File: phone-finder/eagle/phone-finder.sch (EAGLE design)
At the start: 52 parts, among them J1 MICRO USB, J2 SWD HEADER, K1 35701331, Q1 12Mhz, Q2 2N2222, Q3 2N2222, T1 DTA114EET1G (2x10K), U1 AP2114H-3.3TRG1, U2 NUF2042XV6T1G, U3 LPC11U35FHI33/501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

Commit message: Work in progress
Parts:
- Q2: device transistor-npn:BC818-16SMD -> transistor-npn:BC847ALT1SMD
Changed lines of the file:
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@@
 <part name="R12" library="wifi-orb" deviceset="R-US_" device="R0402" value="100"/>
 <part name="R9" library="wifi-orb" deviceset="R-US_" device="R0402" value="100"/>
-<part name="Q2" library="transistor-npn" deviceset="BC818*" device="SMD" technology="-16" value="2N2222"/>
 <part name="+5V4" library="wifi-orb" deviceset="+5V" device=""/>
 <part name="C15" library="wifi-orb" deviceset="CAPACITOR" device="C0603K" value="0.1uF"/>
@@
 <part name="R8" library="wifi-orb" deviceset="R-US_" device="R0402" value="3K"/>
 <part name="C16" library="wifi-orb" deviceset="CAPACITOR" device="C0603K" value="0.1uF"/>
+<part name="Q2" library="transistor-npn" deviceset="BC847*" device="SMD" technology="ALT1" value="2N2222"/>
 </parts>
 <sheets>
@@
 <attribute name="VALUE" x="293.37" y="124.206" size="1.778" layer="96"/>
 </instance>
-<instance part="Q2" gate="G$1" x="297.18" y="132.08" smashed="yes">
-<attribute name="NAME" x="301.752" y="134.112" size="1.778" layer="95"/>
-<attribute name="VALUE" x="301.752" y="130.81" size="1.778" layer="96"/>
-</instance>
 <instance part="+5V4" gate="G$1" x="299.72" y="144.78" rot="MR0"/>
 <instance part="C15" gate="G$1" x="287.02" y="111.76" smashed="yes">
@@
 <attribute name="NAME" x="323.596" y="115.697" size="1.778" layer="95"/>
 <attribute name="VALUE" x="323.85" y="109.601" size="1.778" layer="96"/>
+</instance>
+<instance part="Q2" gate="G$1" x="297.18" y="132.08" smashed="yes">
+<attribute name="NAME" x="301.498" y="131.318" size="1.778" layer="95"/>
+<attribute name="VALUE" x="301.498" y="128.016" size="1.778" layer="96"/>
 </instance>
 </instances>
@@
 </segment>
 <segment>
-<pinref part="Q2" gate="G$1" pin="C"/>
 <wire x1="299.72" y1="137.16" x2="299.72" y2="142.24" width="0.1524" layer="91"/>
 <pinref part="+5V4" gate="G$1" pin="+5V"/>
+<pinref part="Q2" gate="G$1" pin="C"/>
 </segment>
 </net>
@@
 </segment>
 </net>
-<net name="N$21" class="0">
-<segment>
-<pinref part="Q2" gate="G$1" pin="E"/>
-<pinref part="R9" gate="G$1" pin="2"/>
-</segment>
-</net>
 <net name="N$23" class="0">
 <segment>
 <pinref part="C15" gate="G$1" pin="1"/>
 <wire x1="287.02" y1="114.3" x2="287.02" y2="124.46" width="0.1524" layer="91"/>
-<pinref part="Q2" gate="G$1" pin="B"/>
 <wire x1="287.02" y1="124.46" x2="287.02" y2="132.08" width="0.1524" layer="91"/>
 <wire x1="287.02" y1="132.08" x2="294.64" y2="132.08" width="0.1524" layer="91"/>
@@
 <junction x="287.02" y="124.46"/>
 <junction x="287.02" y="132.08"/>
-</segment>
-</net>
+<pinref part="Q2" gate="G$1" pin="B"/>
+</segment>
+</net>
+<net name="N$8" class="0">
+<segment>
+<pinref part="R9" gate="G$1" pin="2"/>
+<pinref part="Q2" gate="G$1" pin="E"/>
+</segment>
+</net>

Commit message: Associated schematic parts with library parts.
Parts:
- ANTENNA, LINE1, LINE2: device pinhead:PINHD-1X1 -> phone-finder:PINHD-1X1
- C1, C2: device wifi-orb:C-USC0402K -> phone-finder:CC0402K
- C10, C11, C13, C15, C16, C17, C3, C4: device wifi-orb:CAPACITORC0603K -> phone-finder:CC0402K
- C12, C14, C9: device wifi-orb:C-US1C0805K -> phone-finder:CC0805K
- C5, C8: device wifi-orb:CPOL-USUD-6,3X5,8 -> phone-finder:C-POLUD-6,3X5,8
- C6, C7: device wifi-orb:CAPACITORC0603K -> phone-finder:CC0603K
- D1: device diode:BZW50B -> phone-finder:DUAL-ZENER
- D2: device wifi-orb:BAS40-05 -> phone-finder:BAS40-05
- J1: device wifi-orb:USB -> phone-finder:USB-CONN
- J2: device wifi-orb:SWD-HEADER -> phone-finder:SWD-HEADER
- K1: value 35701331 -> RELAY; device relay:35701331 -> phone-finder:RELAY
- MH$1, MH$2, MH$3, MH$4: value MOUNTING_HOLE -> MOUNTING-HOLE; device wifi-orb:MOUNTING_HOLE -> phone-finder:MOUNTING-HOLE
- Q1: device wifi-orb:CRYSTALCTS406 -> phone-finder:CRYSTALCTS406
- Q2, Q3: device transistor-npn:BC847ALT1SMD -> phone-finder:NPNALT1SMD
- R1, R11, R2, R3, R4, R5, R6, R7, R8: device wifi-orb:R-US_R0402 -> phone-finder:RR0402
- R10, R12, R9: device wifi-orb:R-US_R0402 -> phone-finder:RR0805
- S1, S2: value PUSH_BUTTON -> PUSH-BUTTON; device wifi-orb:PUSH_BUTTON -> phone-finder:PUSH-BUTTON
- T1: device wifi-orb:PNP_RESISTORS -> phone-finder:PNP-BIASED
- TR1: value PE-65612 -> TRANSFORMER; device transformer-pulse:PE-65612 -> phone-finder:TRANSFORMER
- U1: device wifi-orb:LDOSOT223 -> phone-finder:LDOSOT223
- U2: device wifi-orb:USB_FILTER -> phone-finder:USB-ESD
- U3: device wifi-orb:LPC11U35FHN33/501 -> phone-finder:LPC11U35FHN33/501
- U4: device wifi-orb:WIFI_MODULESMT -> phone-finder:WIFI-MODULESMT

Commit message: Work in progress.
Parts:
- removed LINE1, LINE2: (no value), phone-finder:PINHD-1X1
- added D3: SFH482, led:SFH482
- added J3: SWD HEADER, phone-finder:SWD-HEADER
- added R13: 1K5, phone-finder:RR0402
- J2: value SWD HEADER -> PHONE-JACK; device phone-finder:SWD-HEADER -> phone-finder:PHONE-JACK
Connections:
- removed net N$9 (its old number): K12.S, LINE1.1
- new net LED: R13.1, U3.CT16B1_CAP0/PIO0_20
- new net N$11: J2.2, K12.S
- new net N$14: D3.A, R13.2
- net +3V3: now also J3.1; no longer J2.1
- net GND: now also D3.C, J3.3, J3.5, J3.7, J3.9; no longer J2.3, J2.5, J2.7, J2.9
- net N$10: now also J2.3; no longer LINE2.1
- net RESET: now also J3.10; no longer J2.10
- net SWDCLK: now also J3.4; no longer J2.4
- net SWDIO: now also J3.2; no longer J2.2
- net SWDO: now also J3.6; no longer J2.6
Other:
- moved on the sheet: ANTENNA, C10, C11, C12, C13, C14, C15, C16, C17, C9, D1, D2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

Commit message: Worked in progress. Cleanedup some of the library components.
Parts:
- Q2, Q3: device phone-finder:NPNALT1SMD -> phone-finder:NPN
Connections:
- net +5V: now also K11.COIL-POS; no longer K11.3
- net N$11: now also J2.4, K12.S1; no longer J2.2, K12.S
- net N$20: now also K12.S2; no longer K12.P
- net N$4: now also K11.COIL-NEG; no longer K11.5
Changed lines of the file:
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@@
 <part name="GND27" library="phone-finder" deviceset="GND" device=""/>
 <part name="ANTENNA" library="phone-finder" deviceset="PINHD-1X1" device=""/>
-<part name="Q3" library="phone-finder" deviceset="NPN" device="SMD" technology="ALT1" value="2N2222"/>
+<part name="Q3" library="phone-finder" deviceset="NPN" device="" value="2N2222"/>
 <part name="GND6" library="phone-finder" deviceset="GND" device=""/>
 <part name="K1" library="phone-finder" deviceset="RELAY" device=""/>
@@
 <part name="R8" library="phone-finder" deviceset="R" device="R0402" value="3K"/>
 <part name="C16" library="phone-finder" deviceset="C" device="C0402K" value="0.1uF"/>
-<part name="Q2" library="phone-finder" deviceset="NPN" device="SMD" technology="ALT1" value="2N2222"/>
+<part name="Q2" library="phone-finder" deviceset="NPN" device="" value="2N2222"/>
 <part name="J2" library="phone-finder" deviceset="PHONE-JACK" device=""/>
 <part name="D3" library="led" deviceset="SFH482" device=""/>
@@
 <attribute name="VALUE" x="298.958" y="148.336" size="1.778" layer="96"/>
 </instance>
-<instance part="J2" gate="G$1" x="383.54" y="132.08"/>
+<instance part="J2" gate="G$1" x="383.54" y="132.08" smashed="yes">
+<attribute name="NAME" x="383.54" y="139.7" size="1.778" layer="95"/>
+<attribute name="VALUE" x="378.46" y="123.952" size="1.778" layer="96"/>
+</instance>
 <instance part="D3" gate="1" x="200.66" y="134.62"/>
 <instance part="GND10" gate="1" x="200.66" y="124.46"/>
@@
 </segment>
 <segment>
-<pinref part="K1" gate="1" pin="3"/>
+<pinref part="K1" gate="1" pin="COIL-POS"/>
 <pinref part="+5V3" gate="G$1" pin="+5V"/>
 <wire x1="355.6" y1="116.84" x2="355.6" y2="119.38" width="0.1524" layer="91"/>
@@
 <segment>
 <pinref part="Q3" gate="G$1" pin="C"/>
-<pinref part="K1" gate="1" pin="5"/>
+<pinref part="K1" gate="1" pin="COIL-NEG"/>
 <wire x1="355.6" y1="104.14" x2="355.6" y2="106.68" width="0.1524" layer="91"/>
 </segment>
@@
 <segment>
 <pinref part="R12" gate="G$1" pin="2"/>
-<pinref part="K1" gate="2" pin="P"/>
+<pinref part="K1" gate="2" pin="S2"/>
 <wire x1="355.6" y1="139.7" x2="358.14" y2="139.7" width="0.1524" layer="91"/>
 </segment>
@@
 <net name="N$11" class="0">
 <segment>
-<pinref part="K1" gate="2" pin="S"/>
+<pinref part="K1" gate="2" pin="S1"/>
 <wire x1="373.38" y1="139.7" x2="375.92" y2="139.7" width="0.1524" layer="91"/>
 <wire x1="375.92" y1="139.7" x2="375.92" y2="134.62" width="0.1524" layer="91"/>
-<pinref part="J2" gate="G$1" pin="2"/>
+<pinref part="J2" gate="G$1" pin="4"/>
 <wire x1="375.92" y1="134.62" x2="381" y2="134.62" width="0.1524" layer="91"/>
 </segment>

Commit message: Work in progress.
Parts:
- D3: value SFH482 -> LED; device led:SFH482 -> phone-finder:LED
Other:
- moved on the sheet: C15, C16, D1, J2, J3, K1, Q2, Q3, R10, R11, R12, R4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

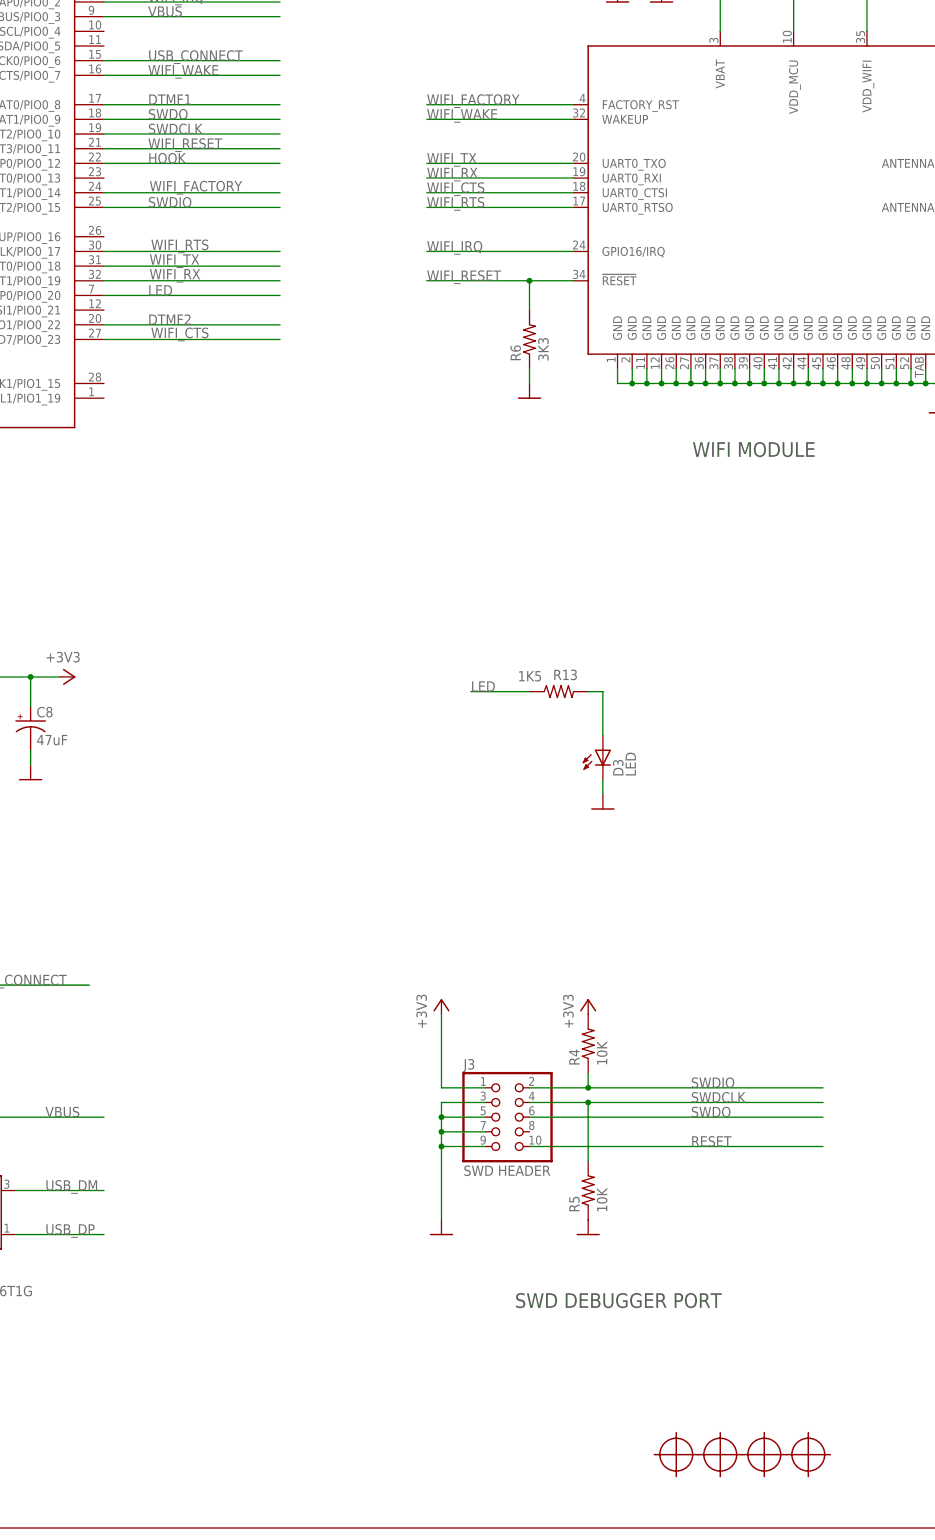
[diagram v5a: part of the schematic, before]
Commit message: Removed the mounting holes. Stable placement.
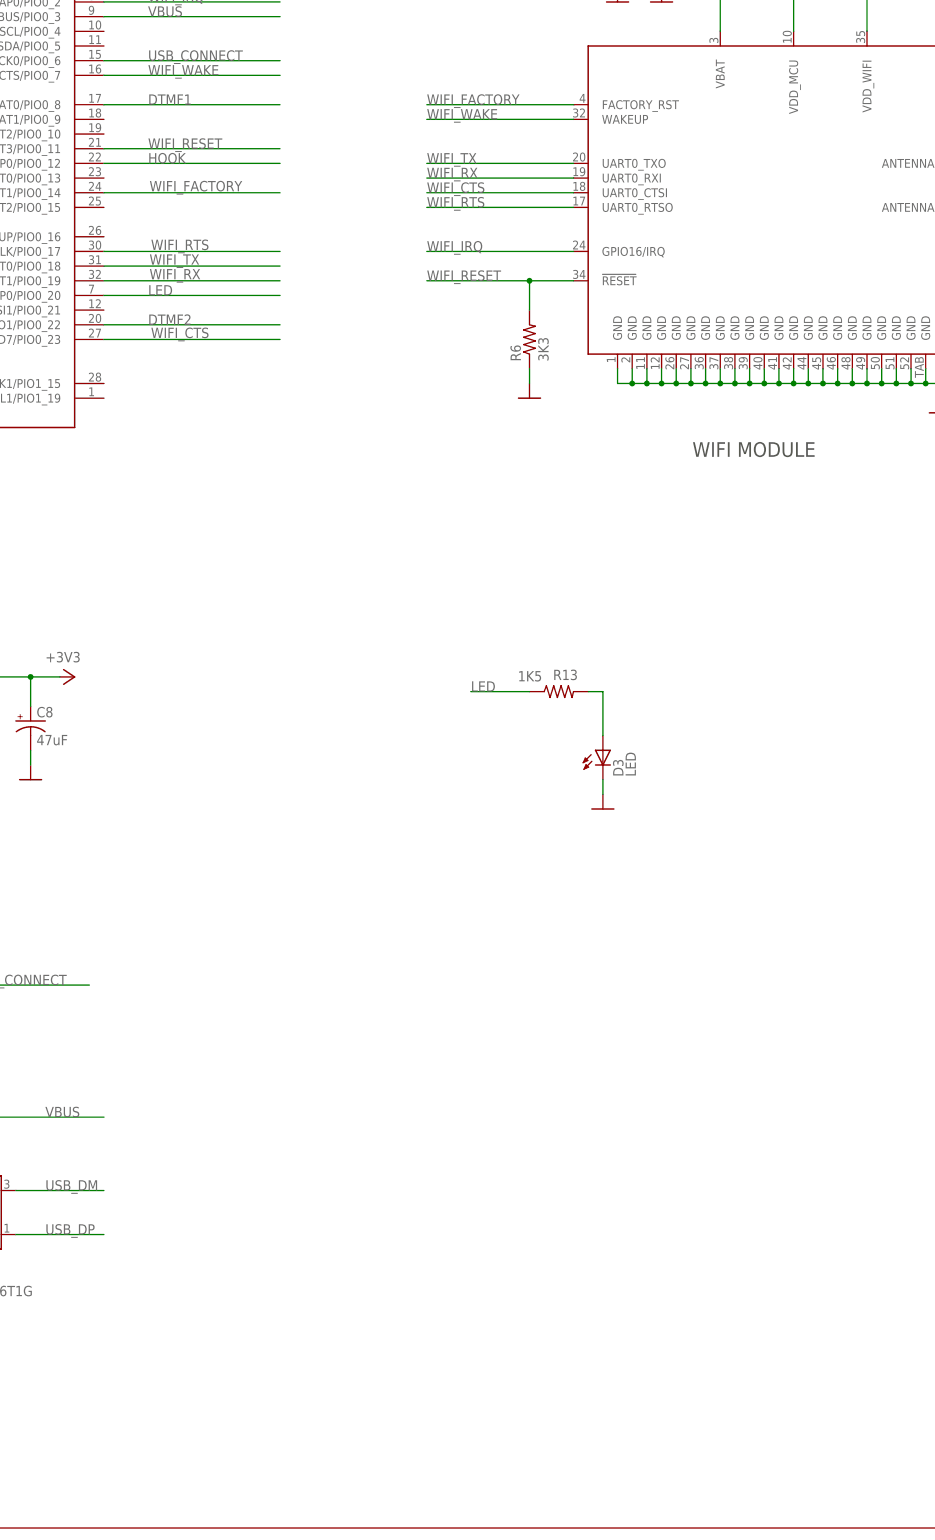
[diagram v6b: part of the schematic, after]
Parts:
- removed J3: SWD HEADER, phone-finder:SWD-HEADER
- removed MH$1, MH$2, MH$3, MH$4: MOUNTING-HOLE, phone-finder:MOUNTING-HOLE
- removed R4, R5: 10K, phone-finder:RR0402
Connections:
- removed net SWDCLK: J3.4, R5.2, U3.SWCLK/SCK0/CT16B0_MAT2/PIO0_10
- removed net SWDIO: J3.2, R4.1, U3.SWDIO/AD4/CT32B1_MAT2/PIO0_15
- removed net SWDO: J3.6, U3.MOSI0/CT16B0_MAT1/PIO0_9
- net +3V3: no longer J3.1, R4.2
- net GND: no longer J3.3, J3.5, J3.7, J3.9, R5.1
- net RESET: no longer J3.10
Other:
- note removed: "SWD DEBUGGER PORT"
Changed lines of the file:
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@@
 <part name="GND5" library="phone-finder" deviceset="GND" device=""/>
 <part name="+5V2" library="phone-finder" deviceset="+5V" device=""/>
-<part name="MH$1" library="phone-finder" deviceset="MOUNTING-HOLE" device=""/>
-<part name="MH$2" library="phone-finder" deviceset="MOUNTING-HOLE" device=""/>
-<part name="MH$3" library="phone-finder" deviceset="MOUNTING-HOLE" device=""/>
-<part name="MH$4" library="phone-finder" deviceset="MOUNTING-HOLE" device=""/>
 <part name="GND22" library="phone-finder" deviceset="GND" device=""/>
 <part name="S1" library="phone-finder" deviceset="PUSH-BUTTON" device=""/>
@@
 <part name="R1" library="phone-finder" deviceset="R" device="R0402" value="1K5"/>
 <part name="+3V5" library="phone-finder" deviceset="+3V3" device=""/>
-<part name="J3" library="phone-finder" deviceset="SWD-HEADER" device="" value="SWD HEADER"/>
-<part name="+3V6" library="phone-finder" deviceset="+3V3" device=""/>
-<part name="GND16" library="phone-finder" deviceset="GND" device=""/>
-<part name="R4" library="phone-finder" deviceset="R" device="R0402" value="10K"/>
-<part name="R5" library="phone-finder" deviceset="R" device="R0402" value="10K"/>
-<part name="GND17" library="phone-finder" deviceset="GND" device=""/>
-<part name="+3V7" library="phone-finder" deviceset="+3V3" device=""/>
 <part name="R3" library="phone-finder" deviceset="R" device="R0402" value="10K"/>
 <part name="+3V8" library="phone-finder" deviceset="+3V3" device=""/>
@@
 <text x="68.58" y="33.02" size="2.54" layer="97">USB</text>
 <text x="73.66" y="177.8" size="2.54" layer="97">MCU</text>
-<text x="185.42" y="38.1" size="2.54" layer="97">SWD DEBUGGER PORT</text>
 <text x="338.074" y="212.09" size="1.778" layer="94">ISP</text>
 <text x="359.41" y="212.344" size="1.778" layer="94">RST</text>
@@
 <text x="330.2" y="190.5" size="2.54" layer="97">LOAD / RUN MODES</text>
 <text x="216.154" y="185.42" size="2.54" layer="97">WIFI MODULE</text>
-<wire x1="162.56" y1="99.06" x2="243.84" y2="99.06" width="0.254" layer="132" style="shortdash"/>
-<wire x1="243.84" y1="99.06" x2="243.84" y2="45.72" width="0.254" layer="132" style="shortdash"/>
-<wire x1="243.84" y1="45.72" x2="162.56" y2="45.72" width="0.254" layer="132" style="shortdash"/>
-<wire x1="162.56" y1="45.72" x2="162.56" y2="99.06" width="0.254" layer="132" style="shortdash"/>
 <wire x1="314.96" y1="198.12" x2="381" y2="198.12" width="0.254" layer="132" style="shortdash"/>
 <wire x1="381" y1="198.12" x2="381" y2="264.16" width="0.254" layer="132" style="shortdash"/>
@@
 <instance part="GND5" gate="1" x="53.34" y="45.72"/>
 <instance part="+5V2" gate="G$1" x="53.34" y="78.74" rot="MR0"/>
-<instance part="MH$1" gate="G$1" x="213.36" y="12.7"/>
-<instance part="MH$2" gate="G$1" x="220.98" y="12.7"/>
-<instance part="MH$3" gate="G$1" x="228.6" y="12.7"/>
-<instance part="MH$4" gate="G$1" x="236.22" y="12.7"/>
 <instance part="GND22" gate="1" x="347.98" y="203.2"/>
 <instance part="S1" gate="G$1" x="347.98" y="213.36" smashed="yes">
@@
 <instance part="R1" gate="G$1" x="63.5" y="81.28" rot="R90"/>
 <instance part="+3V5" gate="G$1" x="109.22" y="147.32" rot="R270"/>
-<instance part="J3" gate="A" x="182.88" y="71.12"/>
-<instance part="+3V6" gate="G$1" x="172.72" y="91.44"/>
-<instance part="GND16" gate="1" x="172.72" y="50.8"/>
-<instance part="R4" gate="G$1" x="198.12" y="83.82" rot="R90"/>
-<instance part="R5" gate="G$1" x="198.12" y="58.42" rot="R90"/>
-<instance part="GND17" gate="1" x="198.12" y="50.8"/>
-<instance part="+3V7" gate="G$1" x="198.12" y="91.44"/>
 <instance part="R3" gate="G$1" x="116.84" y="276.86" smashed="yes" rot="R90">
 <attribute name="NAME" x="119.38" y="278.1046" size="1.778" layer="95"/>
@@
 <wire x1="53.34" y1="50.8" x2="53.34" y2="48.26" width="0.1524" layer="91"/>
 <junction x="53.34" y="50.8"/>
-</segment>
-<segment>
-<pinref part="J3" gate="A" pin="3"/>
-<pinref part="GND16" gate="1" pin="GND"/>
-<wire x1="180.34" y1="73.66" x2="172.72" y2="73.66" width="0.1524" layer="91"/>
-<wire x1="172.72" y1="73.66" x2="172.72" y2="71.12" width="0.1524" layer="91"/>
-<pinref part="J3" gate="A" pin="5"/>
-<wire x1="172.72" y1="71.12" x2="172.72" y2="68.58" width="0.1524" layer="91"/>
-<wire x1="172.72" y1="68.58" x2="172.72" y2="66.04" width="0.1524" layer="91"/>
-<wire x1="172.72" y1="66.04" x2="172.72" y2="53.34" width="0.1524" layer="91"/>
-<wire x1="180.34" y1="71.12" x2="172.72" y2="71.12" width="0.1524" layer="91"/>
-<pinref part="J3" gate="A" pin="7"/>
-<wire x1="180.34" y1="68.58" x2="172.72" y2="68.58" width="0.1524" layer="91"/>
-<pinref part="J3" gate="A" pin="9"/>
-<wire x1="180.34" y1="66.04" x2="172.72" y2="66.04" width="0.1524" layer="91"/>
-<junction x="172.72" y="71.12"/>
-<junction x="172.72" y="68.58"/>
-<junction x="172.72" y="66.04"/>
-</segment>
-<segment>
-<pinref part="R5" gate="G$1" pin="1"/>
-<pinref part="GND17" gate="1" pin="GND"/>
 </segment>
 <segment>
@@
 </segment>
 <segment>
-<pinref part="J3" gate="A" pin="1"/>
-<pinref part="+3V6" gate="G$1" pin="+3V3"/>
-<wire x1="180.34" y1="76.2" x2="172.72" y2="76.2" width="0.1524" layer="91"/>
-<wire x1="172.72" y1="76.2" x2="172.72" y2="88.9" width="0.1524" layer="91"/>
-</segment>
-<segment>
-<pinref part="R4" gate="G$1" pin="2"/>
-<pinref part="+3V7" gate="G$1" pin="+3V3"/>
-</segment>
-<segment>
 <pinref part="R3" gate="G$1" pin="2"/>
 <pinref part="+3V8" gate="G$1" pin="+3V3"/>
@@
 <net name="RESET" class="0">
 <segment>
-<pinref part="J3" gate="A" pin="10"/>
-<wire x1="187.96" y1="66.04" x2="238.76" y2="66.04" width="0.1524" layer="91"/>
-<label x="215.9" y="66.04" size="1.778" layer="95"/>
-</segment>
-<segment>
 <pinref part="U3" gate="G$1" pin="RESET/PIO0_0"/>
 <wire x1="114.3" y1="269.24" x2="116.84" y2="269.24" width="0.1524" layer="91"/>
@@
 </segment>
 </net>
-<net name="SWDIO" class="0">
-<segment>
-<pinref part="J3" gate="A" pin="2"/>
-<wire x1="187.96" y1="76.2" x2="198.12" y2="76.2" width="0.1524" layer="91"/>
-<pinref part="R4" gate="G$1" pin="1"/>
-<wire x1="198.12" y1="76.2" x2="238.76" y2="76.2" width="0.1524" layer="91"/>
-<wire x1="198.12" y1="78.74" x2="198.12" y2="76.2" width="0.1524" layer="91"/>
-<junction x="198.12" y="76.2"/>
-<label x="215.9" y="76.2" size="1.778" layer="95"/>
-</segment>
-<segment>
-<pinref part="U3" gate="G$1" pin="SWDIO/AD4/CT32B1_MAT2/PIO0_15"/>
-<wire x1="114.3" y1="228.6" x2="144.78" y2="228.6" width="0.1524" layer="91"/>
-<label x="121.92" y="228.6" size="1.778" layer="95"/>
-</segment>
-</net>
 <net name="ISP_EN" class="0">
 <segment>
@@
 </segment>
 </net>
-<net name="SWDO" class="0">
-<segment>
-<pinref part="J3" gate="A" pin="6"/>
-<wire x1="187.96" y1="71.12" x2="238.76" y2="71.12" width="0.1524" layer="91"/>
-<label x="215.9" y="71.12" size="1.778" layer="95"/>
-</segment>
-<segment>
-<pinref part="U3" gate="G$1" pin="MOSI0/CT16B0_MAT1/PIO0_9"/>
-<wire x1="114.3" y1="243.84" x2="144.78" y2="243.84" width="0.1524" layer="91"/>
-<label x="121.92" y="243.84" size="1.778" layer="95"/>
-</segment>
-</net>
 <net name="N$12" class="2">
 <segment>
@@
 </segment>
 </net>
-<net name="SWDCLK" class="0">
-<segment>
-<pinref part="U3" gate="G$1" pin="SWCLK/SCK0/CT16B0_MAT2/PIO0_10"/>
-<wire x1="114.3" y1="241.3" x2="144.78" y2="241.3" width="0.1524" layer="91"/>
-<label x="121.92" y="241.3" size="1.778" layer="95"/>
-</segment>
-<segment>
-<pinref part="J3" gate="A" pin="4"/>
-<wire x1="187.96" y1="73.66" x2="198.12" y2="73.66" width="0.1524" layer="91"/>
-<pinref part="R5" gate="G$1" pin="2"/>
-<wire x1="198.12" y1="73.66" x2="238.76" y2="73.66" width="0.1524" layer="91"/>
-<wire x1="198.12" y1="73.66" x2="198.12" y2="63.5" width="0.1524" layer="91"/>
-<junction x="198.12" y="73.66"/>
-<label x="215.9" y="73.66" size="1.778" layer="95"/>
-</segment>
-</net>
